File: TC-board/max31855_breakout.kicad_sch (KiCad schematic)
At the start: 6 parts

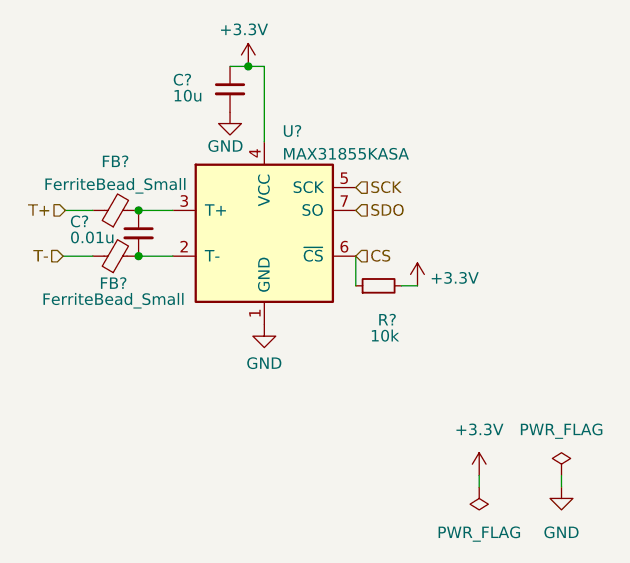
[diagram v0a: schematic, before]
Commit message: Ironing out small details, changed pcf8575 to IC instead of breakout.
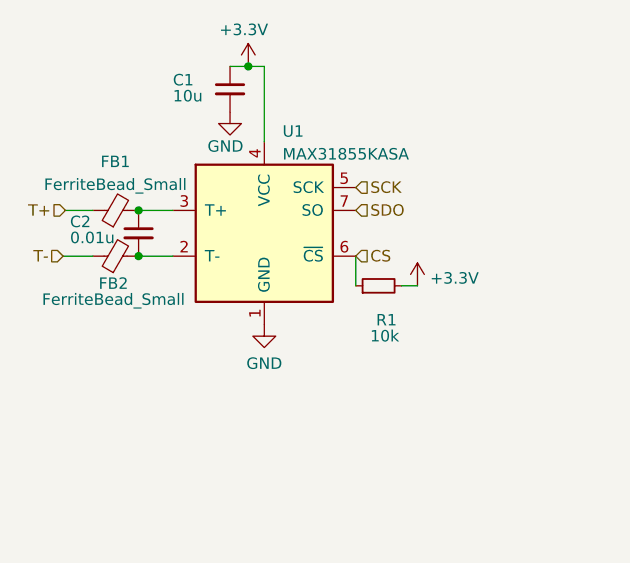
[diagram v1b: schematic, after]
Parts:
- C1, C2: renamed from C?; footprint (none) -> Capacitor_SMD:C_0603_1608Metric
- FB1, FB2: renamed from FB?; footprint (none) -> Capacitor_SMD:C_0603_1608Metric
- R1: renamed from R?; footprint (none) -> Resistor_SMD:R_0603_1608Metric
- gave numbers to parts that had none: 1
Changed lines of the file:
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@@
-    (stroke (width 0) (type default) (color 0 0 0 0))
-  )
-  (wire (pts (xy 115.824 92.71) (xy 115.824 93.98))
     (stroke (width 0) (type default) (color 0 0 0 0))
   )
@@
   )
   (wire (pts (xy 60.452 68.326) (xy 63.754 68.326))
-    (stroke (width 0) (type default) (color 0 0 0 0))
-  )
-  (wire (pts (xy 106.68 93.98) (xy 106.68 92.71))
     (stroke (width 0) (type default) (color 0 0 0 0))
   )
@@
   (symbol (lib_id "Sensor_Temperature:MAX31855KASA") (at 82.804 65.786 0) (unit 1)
     (in_bom yes) (on_board yes) (fields_autoplaced)
-    (property "Reference" "U?" (id 0) (at 84.8234 54.4662 0)
+    (property "Reference" "U1" (id 0) (at 84.8234 54.4662 0)
       (effects (font (size 1.27 1.27)) (justify left))
     )
@@
   (symbol (lib_id "power:+3.3V") (at 99.822 71.628 0) (unit 1)
     (in_bom yes) (on_board yes) (fields_autoplaced)
-    (property "Reference" "#PWR?" (id 0) (at 99.822 75.438 0)
+    (property "Reference" "#PWR09" (id 0) (at 99.822 75.438 0)
       (effects (font (size 1.27 1.27)) hide)
     )
@@
   (symbol (lib_id "Device:C_Small") (at 68.834 65.786 0) (unit 1)
     (in_bom yes) (on_board yes)
-    (property "Reference" "C?" (id 0) (at 61.214 64.516 0)
+    (property "Reference" "C2" (id 0) (at 61.214 64.516 0)
       (effects (font (size 1.27 1.27)) (justify left))
     )
@@
       (effects (font (size 1.27 1.27)) (justify left))
     )
-    (property "Footprint" "" (id 2) (at 68.834 65.786 0)
+    (property "Footprint" "Capacitor_SMD:C_0603_1608Metric" (id 2) (at 68.834 65.786 0)
       (effects (font (size 1.27 1.27)) hide)
     )
@@
   (symbol (lib_id "power:+3.3V") (at 81.026 47.244 0) (unit 1)
     (in_bom yes) (on_board yes)
-    (property "Reference" "#PWR?" (id 0) (at 81.026 51.054 0)
+    (property "Reference" "#PWR07" (id 0) (at 81.026 51.054 0)
       (effects (font (size 1.27 1.27)) hide)
     )
@@
   (symbol (lib_id "power:GND") (at 82.804 75.946 0) (unit 1)
     (in_bom yes) (on_board yes)
-    (property "Reference" "#PWR?" (id 0) (at 82.804 82.296 0)
+    (property "Reference" "#PWR010" (id 0) (at 82.804 82.296 0)
       (effects (font (size 1.27 1.27)) hide)
     )
@@
   (symbol (lib_id "Device:R_Small") (at 95.504 71.628 90) (unit 1)
     (in_bom yes) (on_board yes)
-    (property "Reference" "R?" (id 0) (at 97.536 75.438 90)
+    (property "Reference" "R1" (id 0) (at 97.536 75.438 90)
       (effects (font (size 1.27 1.27)) (justify left))
     )
@@
       (effects (font (size 1.27 1.27)) (justify left))
     )
-    (property "Footprint" "" (id 2) (at 95.504 71.628 0)
+    (property "Footprint" "Resistor_SMD:R_0603_1608Metric" (id 2) (at 95.504 71.628 0)
       (effects (font (size 1.27 1.27)) hide)
     )
@@
   (symbol (lib_id "Device:FerriteBead_Small") (at 66.294 68.326 90) (unit 1)
     (in_bom yes) (on_board yes)
-    (property "Reference" "FB?" (id 0) (at 66.04 71.374 90))
+    (property "Reference" "FB2" (id 0) (at 66.04 71.374 90))
     (property "Value" "FerriteBead_Small" (id 1) (at 66.04 73.152 90))
-    (property "Footprint" "" (id 2) (at 66.294 70.104 90)
+    (property "Footprint" "Capacitor_SMD:C_0603_1608Metric" (id 2) (at 66.294 70.104 90)
       (effects (font (size 1.27 1.27)) hide)
     )
@@
     (pin "2")
   )
-  (symbol (lib_id "power:PWR_FLAG") (at 115.824 92.71 0) (unit 1)
-    (in_bom yes) (on_board yes) (fields_autoplaced)
-    (property "Reference" "#FLG?" (id 0) (at 115.824 90.805 0)
-      (effects (font (size 1.27 1.27)) hide)
-    )
-    (property "Value" "PWR_FLAG" (id 1) (at 115.824 87.63 0))
-    (property "Footprint" "" (id 2) (at 115.824 92.71 0)
-      (effects (font (size 1.27 1.27)) hide)
-    )
-    (property "Datasheet" "~" (id 3) (at 115.824 92.71 0)
-      (effects (font (size 1.27 1.27)) hide)
-    )
-    (pin "1")
-  )
-  (symbol (lib_id "power:+3.3V") (at 106.68 92.71 0) (unit 1)
-    (in_bom yes) (on_board yes) (fields_autoplaced)
-    (property "Reference" "#PWR?" (id 0) (at 106.68 96.52 0)
-      (effects (font (size 1.27 1.27)) hide)
-    )
-    (property "Value" "+3.3V" (id 1) (at 106.68 87.63 0))
-    (property "Footprint" "" (id 2) (at 106.68 92.71 0)
-      (effects (font (size 1.27 1.27)) hide)
-    )
-    (property "Datasheet" "" (id 3) (at 106.68 92.71 0)
-      (effects (font (size 1.27 1.27)) hide)
-    )
-    (pin "1")
-  )
-  (symbol (lib_id "power:GND") (at 115.824 93.98 0) (unit 1)
-    (in_bom yes) (on_board yes) (fields_autoplaced)
-    (property "Reference" "#PWR?" (id 0) (at 115.824 100.33 0)
-      (effects (font (size 1.27 1.27)) hide)
-    )
-    (property "Value" "GND" (id 1) (at 115.824 99.06 0))
-    (property "Footprint" "" (id 2) (at 115.824 93.98 0)
-      (effects (font (size 1.27 1.27)) hide)
-    )
-    (property "Datasheet" "" (id 3) (at 115.824 93.98 0)
-      (effects (font (size 1.27 1.27)) hide)
-    )
-    (pin "1")
-  )
   (symbol (lib_id "Device:FerriteBead_Small") (at 66.294 63.246 90) (unit 1)
     (in_bom yes) (on_board yes) (fields_autoplaced)
-    (property "Reference" "FB?" (id 0) (at 66.2559 57.8444 90))
+    (property "Reference" "FB1" (id 0) (at 66.2559 57.8444 90))
     (property "Value" "FerriteBead_Small" (id 1) (at 66.2559 60.3813 90))
-    (property "Footprint" "" (id 2) (at 66.294 65.024 90)
+    (property "Footprint" "Capacitor_SMD:C_0603_1608Metric" (id 2) (at 66.294 65.024 90)
       (effects (font (size 1.27 1.27)) hide)
     )
@@
   (symbol (lib_id "power:GND") (at 78.994 52.324 0) (unit 1)
     (in_bom yes) (on_board yes)
-    (property "Reference" "#PWR?" (id 0) (at 78.994 58.674 0)
+    (property "Reference" "#PWR08" (id 0) (at 78.994 58.674 0)
       (effects (font (size 1.27 1.27)) hide)
     )
@@
   (symbol (lib_id "Device:C_Small") (at 78.994 49.784 0) (unit 1)
     (in_bom yes) (on_board yes)
-    (property "Reference" "C?" (id 0) (at 72.644 48.768 0)
+    (property "Reference" "C1" (id 0) (at 72.644 48.768 0)
       (effects (font (size 1.27 1.27)) (justify left))
     )
@@
       (effects (font (size 1.27 1.27)) (justify left))
     )
-    (property "Footprint" "" (id 2) (at 78.994 49.784 0)
+    (property "Footprint" "Capacitor_SMD:C_0603_1608Metric" (id 2) (at 78.994 49.784 0)
       (effects (font (size 1.27 1.27)) hide)
     )
@@
     (pin "2")
   )
-  (symbol (lib_id "power:PWR_FLAG") (at 106.68 93.98 180) (unit 1)
-    (in_bom yes) (on_board yes) (fields_autoplaced)
-    (property "Reference" "#FLG?" (id 0) (at 106.68 95.885 0)
-      (effects (font (size 1.27 1.27)) hide)
-    )
-    (property "Value" "PWR_FLAG" (id 1) (at 106.68 99.06 0))
-    (property "Footprint" "" (id 2) (at 106.68 93.98 0)
-      (effects (font (size 1.27 1.27)) hide)
-    )
-    (property "Datasheet" "~" (id 3) (at 106.68 93.98 0)
-      (effects (font (size 1.27 1.27)) hide)
-    )
-    (pin "1")
-  )
 )
